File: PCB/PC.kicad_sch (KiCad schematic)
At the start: 11 parts, among them U29 74LS245, U30 74LS161

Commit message: Cleaned up the schematic and got started on assigning all the footprints to the symbols
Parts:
- C15: footprint (none) -> Capacitor_THT:C_Radial_D5.0mm_H5.0mm_P2.00mm
- D34, D35, D36, D37: footprint (none) -> LED_THT:LED_D1.8mm_W1.8mm_H2.4mm_Horizontal_O1.27mm_Z1.6mm
- R33, R34, R35, R36: footprint (none) -> Resistor_THT:R_Axial_DIN0207_L6.3mm_D2.5mm_P7.62mm_Horizontal
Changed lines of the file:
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@@
 			)
 		)
-		(property "Footprint" ""
+		(property "Footprint" "Resistor_THT:R_Axial_DIN0207_L6.3mm_D2.5mm_P7.62mm_Horizontal"
 			(at 62.992 27.94 90)
 			(effects
@@
 			)
 		)
-		(property "Footprint" ""
+		(property "Footprint" "LED_THT:LED_D1.8mm_W1.8mm_H2.4mm_Horizontal_O1.27mm_Z1.6mm"
 			(at 83.82 43.18 0)
 			(effects
@@
 			)
 		)
-		(property "Footprint" ""
+		(property "Footprint" "Resistor_THT:R_Axial_DIN0207_L6.3mm_D2.5mm_P7.62mm_Horizontal"
 			(at 73.152 27.94 90)
 			(effects
@@
 			)
 		)
-		(property "Footprint" ""
+		(property "Footprint" "LED_THT:LED_D1.8mm_W1.8mm_H2.4mm_Horizontal_O1.27mm_Z1.6mm"
 			(at 64.77 43.18 0)
 			(effects
@@
 			)
 		)
-		(property "Footprint" ""
+		(property "Footprint" "LED_THT:LED_D1.8mm_W1.8mm_H2.4mm_Horizontal_O1.27mm_Z1.6mm"
 			(at 91.44 43.18 0)
 			(effects
@@
 			)
 		)
-		(property "Footprint" ""
+		(property "Footprint" "Capacitor_THT:C_Radial_D5.0mm_H5.0mm_P2.00mm"
 			(at 134.3152 26.67 0)
 			(effects
@@
 			)
 		)
-		(property "Footprint" ""
+		(property "Footprint" "Resistor_THT:R_Axial_DIN0207_L6.3mm_D2.5mm_P7.62mm_Horizontal"
 			(at 82.042 27.94 90)
 			(effects
@@
 			)
 		)
-		(property "Footprint" ""
+		(property "Footprint" "Resistor_THT:R_Axial_DIN0207_L6.3mm_D2.5mm_P7.62mm_Horizontal"
 			(at 89.662 27.94 90)
 			(effects
@@
 			)
 		)
-		(property "Footprint" ""
+		(property "Footprint" "LED_THT:LED_D1.8mm_W1.8mm_H2.4mm_Horizontal_O1.27mm_Z1.6mm"
 			(at 74.93 43.18 0)
 			(effects

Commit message: added more models to work with on my pcb
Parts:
- D34, D35, D36: footprint LED_THT:LED_D1.8mm_W1.8mm_H2.4mm_Horizontal_O1.27mm_Z1.6mm -> LED_THT:LED_D3.0mm
- D37: value LED -> GREEN; footprint LED_THT:LED_D1.8mm_W1.8mm_H2.4mm_Horizontal_O1.27mm_Z1.6mm -> LED_THT:LED_D3.0mm
- U29: footprint (none) -> Custom:DIP254P762X508-20
- U30: footprint (none) -> Custom:N16
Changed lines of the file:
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@@
 			)
 		)
-		(property "Footprint" "LED_THT:LED_D1.8mm_W1.8mm_H2.4mm_Horizontal_O1.27mm_Z1.6mm"
+		(property "Footprint" "LED_THT:LED_D3.0mm"
 			(at 83.82 43.18 0)
 			(effects
@@
 			)
 		)
-		(property "Footprint" ""
+		(property "Footprint" "Custom:DIP254P762X508-20"
 			(at 49.53 59.69 0)
 			(effects
@@
 			)
 		)
-		(property "Footprint" ""
+		(property "Footprint" "Custom:N16"
 			(at 107.95 52.07 0)
 			(effects
@@
 			)
 		)
-		(property "Footprint" "LED_THT:LED_D1.8mm_W1.8mm_H2.4mm_Horizontal_O1.27mm_Z1.6mm"
+		(property "Footprint" "LED_THT:LED_D3.0mm"
 			(at 64.77 43.18 0)
 			(effects
@@
 			)
 		)
-		(property "Value" "LED"
+		(property "Value" "GREEN"
 			(at 93.98 42.8624 90)
 			(effects
@@
 			)
 		)
-		(property "Footprint" "LED_THT:LED_D1.8mm_W1.8mm_H2.4mm_Horizontal_O1.27mm_Z1.6mm"
+		(property "Footprint" "LED_THT:LED_D3.0mm"
 			(at 91.44 43.18 0)
 			(effects
@@
 			)
 		)
-		(property "Footprint" "LED_THT:LED_D1.8mm_W1.8mm_H2.4mm_Horizontal_O1.27mm_Z1.6mm"
+		(property "Footprint" "LED_THT:LED_D3.0mm"
 			(at 74.93 43.18 0)
 			(effects

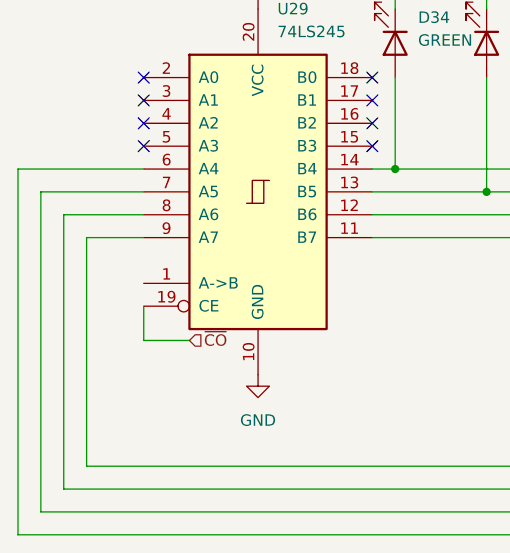
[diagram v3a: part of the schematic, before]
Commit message: Fixed a bunch of ERC errors so know there is only one remaining.
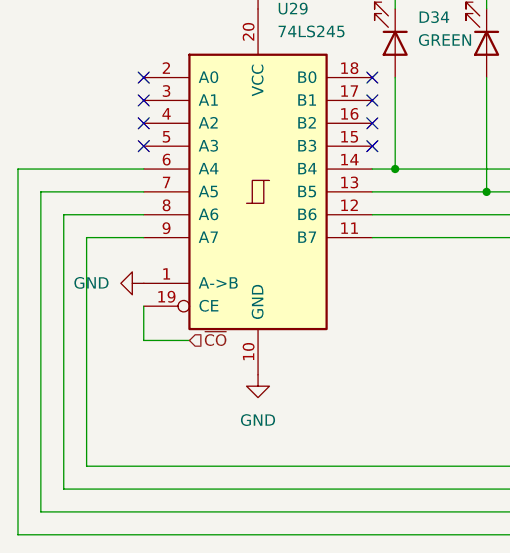
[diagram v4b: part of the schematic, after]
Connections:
- net GND: now also U29.1 (A->B)
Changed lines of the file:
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@@
+	(symbol
+		(lib_id "power:GND")
+		(at 36.83 69.85 270)
+		(unit 1)
+		(exclude_from_sim no)
+		(in_bom yes)
+		(on_board yes)
+		(dnp no)
+		(fields_autoplaced yes)
+		(property "Reference" "#PWR0156"
+			(at 30.48 69.85 0)
+			(effects
+				(font
+					(size 1.27 1.27)
+				)
+				(hide yes)
+			)
+		)
+		(property "Value" "GND"
+			(at 33.02 69.8499 90)
+			(effects
+				(font
+					(size 1.27 1.27)
+				)
+				(justify right)
+			)
+		)
+		(property "Footprint" ""
+			(at 36.83 69.85 0)
+			(effects
+				(font
+					(size 1.27 1.27)
+				)
+				(hide yes)
+			)
+		)
+		(property "Datasheet" ""
+			(at 36.83 69.85 0)
+			(effects
+				(font
+					(size 1.27 1.27)
+				)
+				(hide yes)
+			)
+		)
+		(property "Description" "Power symbol creates a global label with name \"GND\" , ground"
+			(at 36.83 69.85 0)
+			(effects
+				(font
+					(size 1.27 1.27)
+				)
+				(hide yes)
+			)
+		)
+		(pin "1"
+		)
+		(instances
+			(project ""
+				(path "/48633dea-2de9-4b6f-aeff-2ee54233f918/dad9cd65-e3a7-49ca-8062-7aceccd968fb"
+					(reference "#PWR0156")
+					(unit 1)
+				)
+			)
+		)
+	)
 	(symbol
 		(lib_id "power:GND")

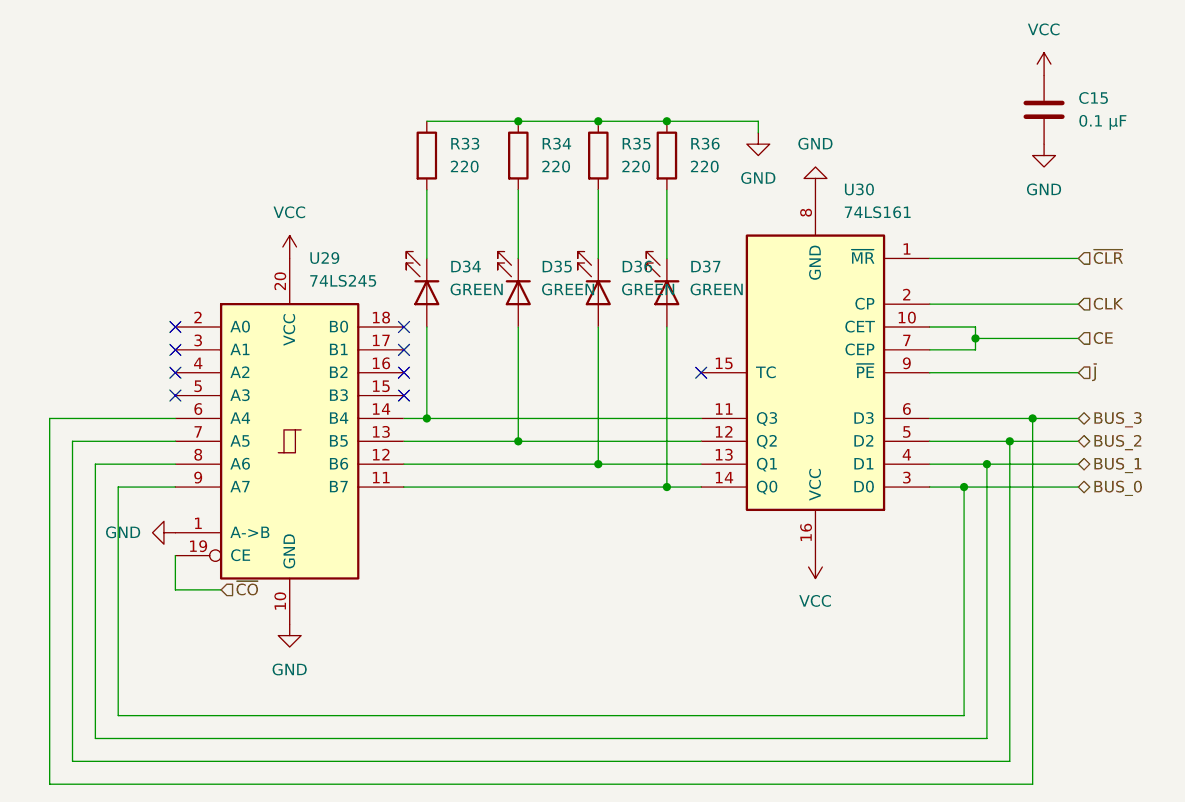
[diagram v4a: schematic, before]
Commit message: Add decupling caps and reroute pcb. Updated BOM to match new number of caps
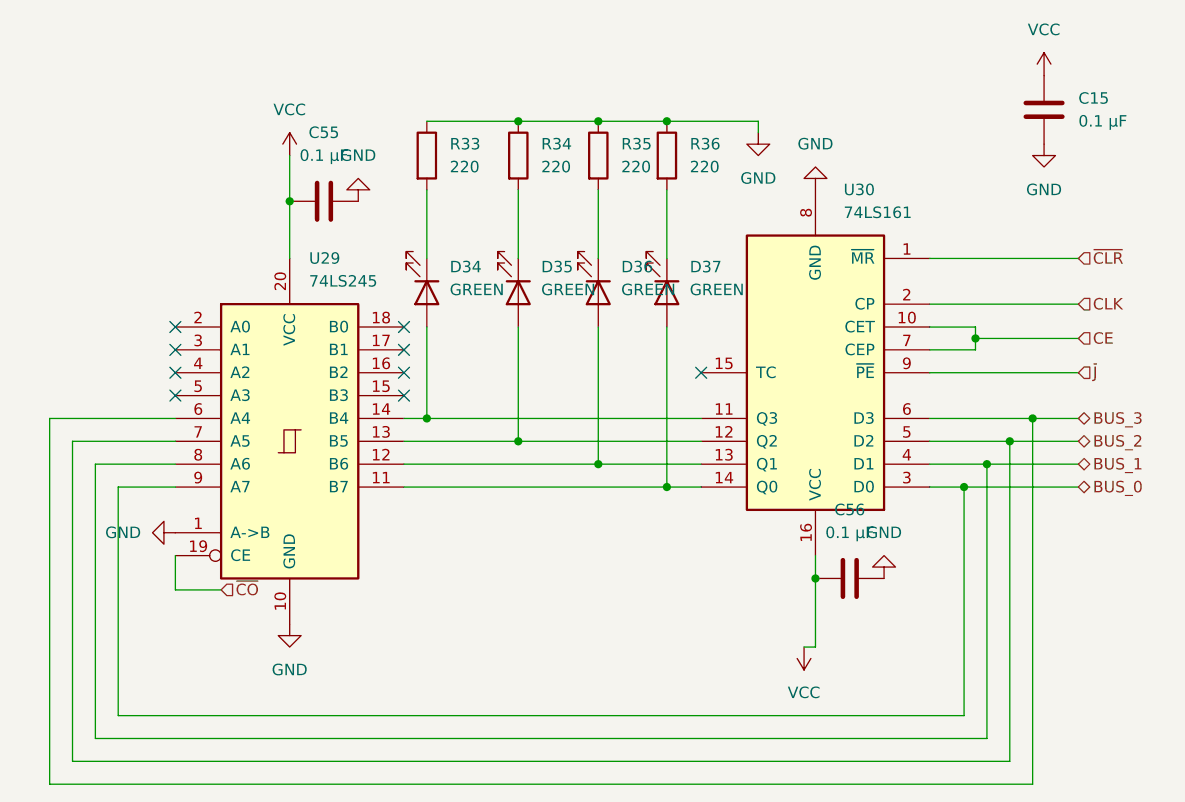
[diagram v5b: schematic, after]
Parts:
- added C55, C56: 0.1 µF, Capacitor_THT:C_Radial_D5.0mm_H5.0mm_P2.00mm, symbol Device:C
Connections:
- net GND: now also C55.2, C56.2
- net VCC: now also C55.1, C56.1

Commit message: Redoing PCB layout and fixed some signal flow convention errors
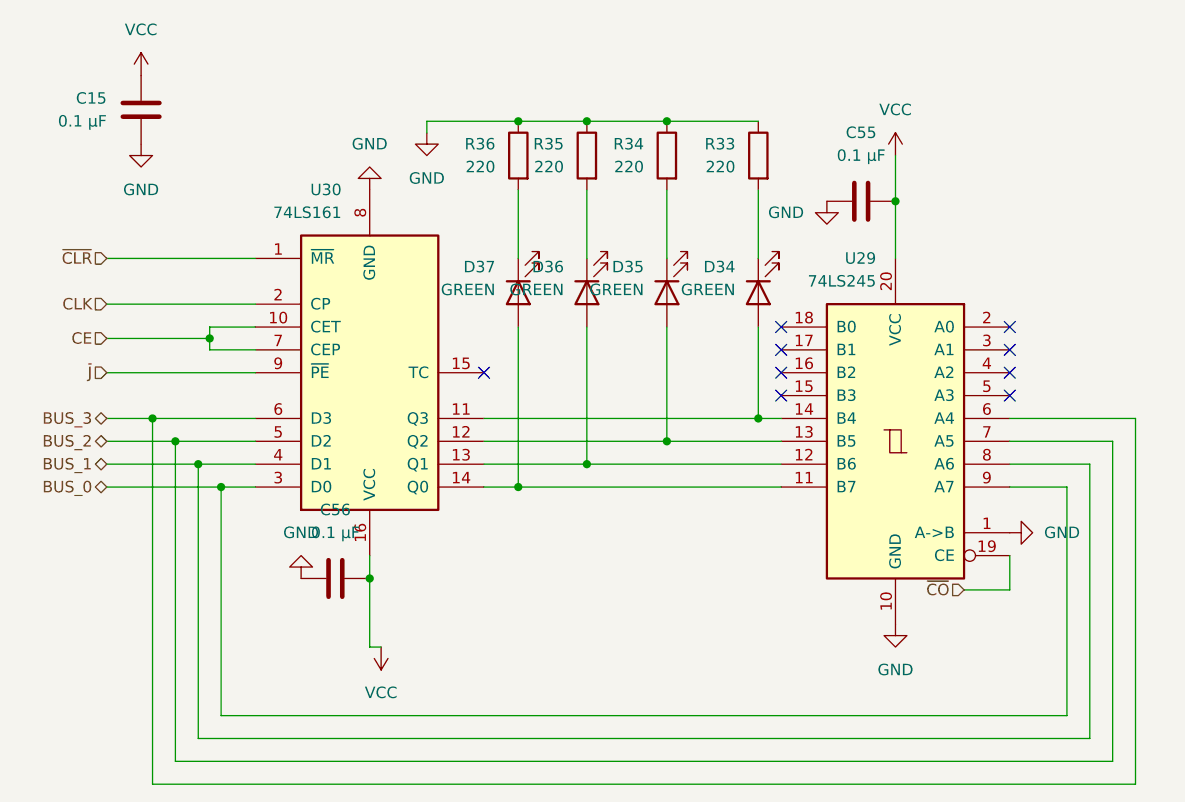
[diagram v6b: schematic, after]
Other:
- moved on the sheet: C15, C55, C56, D34, D35, D36, D37, R33, R34, R35, R36, U29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
